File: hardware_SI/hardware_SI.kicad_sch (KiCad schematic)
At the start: 2 parts, among them U1 OMEGA2+

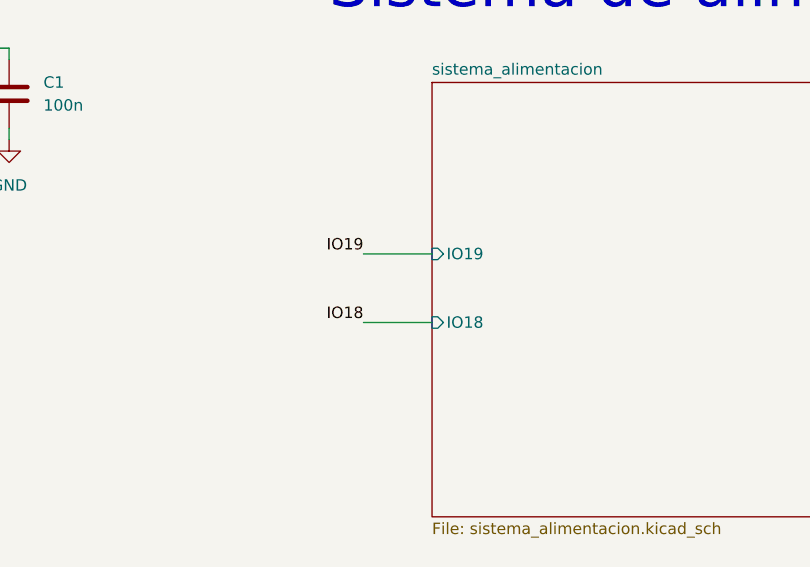
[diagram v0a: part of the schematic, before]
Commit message: Cambio en alimentación y zona GNDPWR
- Debido a los tiempos de entrega del LTC4085, se cambia el sistema de alimentación, agregando un selector automático de fuente y un integrado de manejo de batería.
- En consecuencia de lo anterior, se usa un LDO con menor voltaje de dropout.
- Se cambia el convertidor DC-DC debido a su alto precio.
- En cuanto a PCB, se completa el circuito del convertidor DC-DC y la zona de GNPWR.
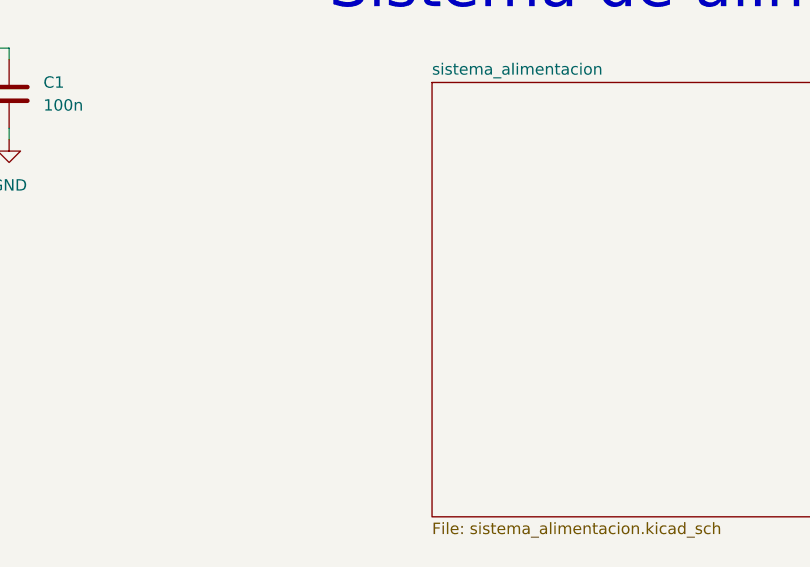
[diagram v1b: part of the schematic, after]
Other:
- sheet sistema_alimentacion ports: added none; removed IO18, IO19
